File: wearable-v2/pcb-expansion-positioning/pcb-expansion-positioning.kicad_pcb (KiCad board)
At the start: 2 copper layers, 35.1 x 19 mm, 18 parts, among them IC1 TESEO-LIV3F, J8 HERALD_V2_CONN_PLUG, U14 LIS2DE12

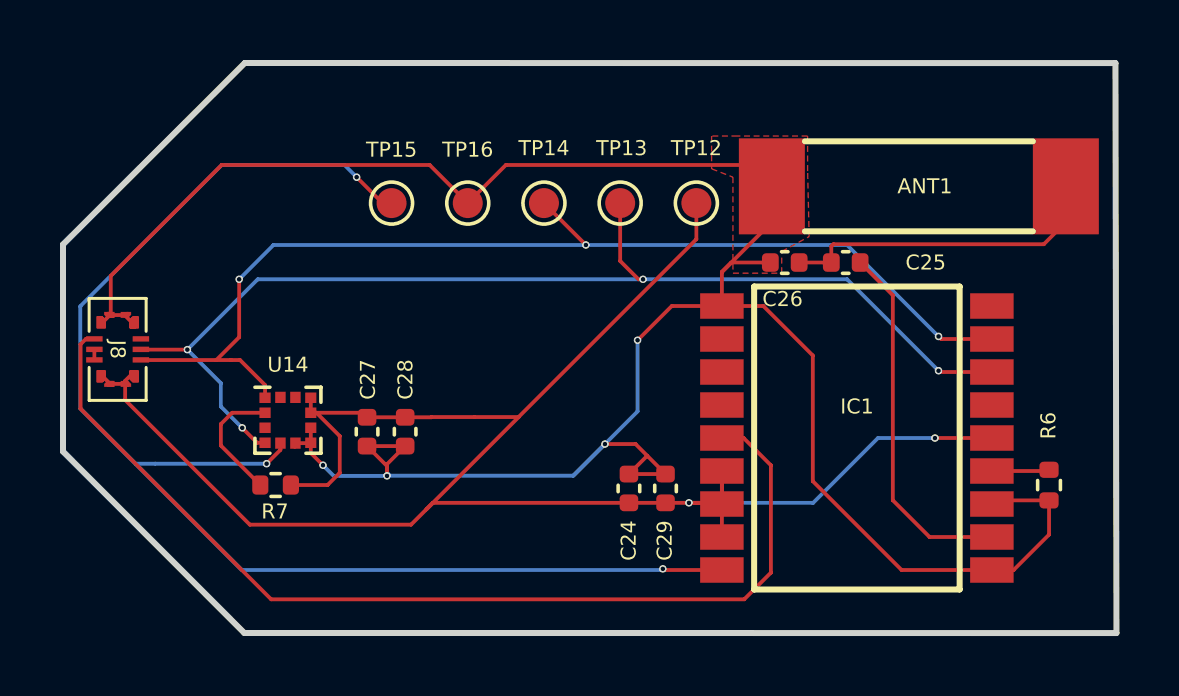
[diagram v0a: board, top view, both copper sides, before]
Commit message: Reworked boards for JLCPCB manufacture
Slightly larger Vias.
Added debug pin holes for Beta testing.
Signed-off-by: Adam Fowler <adam@adamfowler.org>
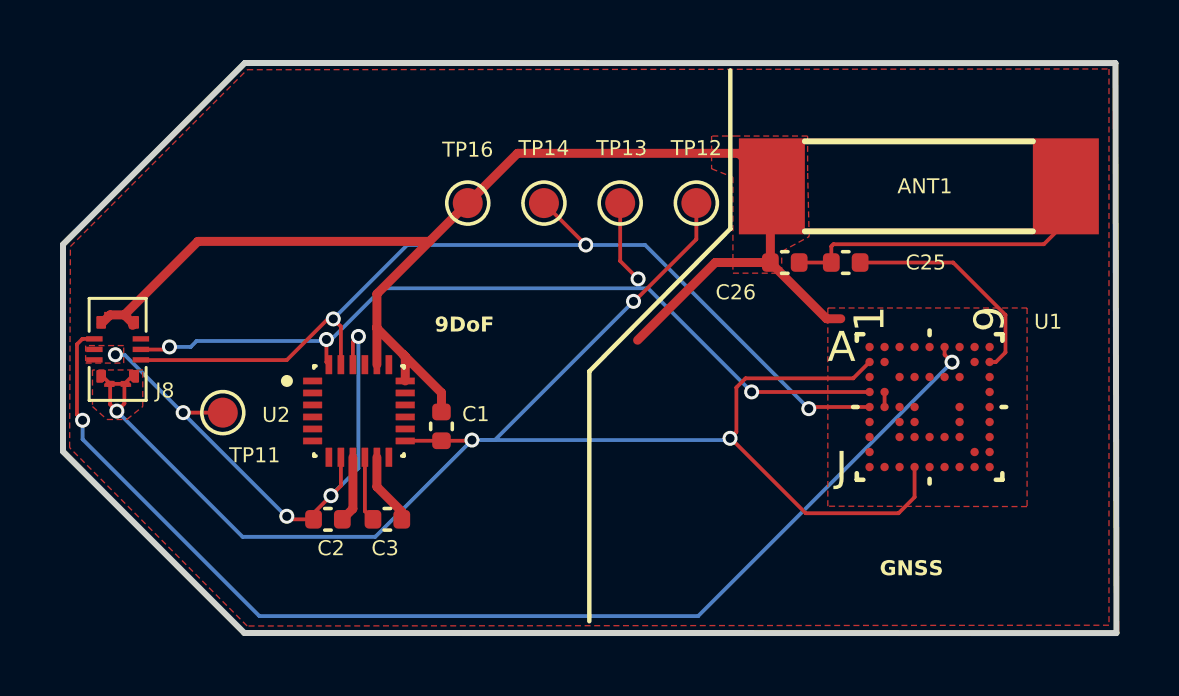
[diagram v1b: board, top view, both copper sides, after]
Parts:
- removed BoardPositioning: Board Positioning, PCM_kikit:Board
- removed C24: 56pF, Capacitor_SMD:C_0402_1005Metric
- removed C27: 10uF, Capacitor_SMD:C_0402_1005Metric
- removed C28, C29: 100nF, Capacitor_SMD:C_0402_1005Metric
- removed IC1: TESEO-LIV3F, Herald:SON110P970X1010X230-18N
- removed R6, R7: 10k, Resistor_SMD:R_0402_1005Metric
- removed TP15: POS_RESETn, TestPoint:TestPoint_Pad_D1.0mm
- removed U14: LIS2DE12, Package_LGA:LGA-12_2x2mm_P0.5mm
- added C1: 100nF, Capacitor_SMD:C_0402_1005Metric, F.Cu at (131.2, 99.1)
- added C2: 100nF, Capacitor_SMD:C_0402_1005Metric, F.Cu at (127.4, 102.2)
- added C3: 100nF, Capacitor_SMD:C_0402_1005Metric, F.Cu at (129.4, 102.2)
- added TP11: VDD1, TestPoint:TestPoint_Pad_D1.0mm, F.Cu at (123.9, 98.6)
- added U1: MIA-M10Q-00B, Herald:LGA_M10Q-00B_UBL, F.Cu at (147.5, 98.4)
- added U2: ICM-20948, Herald:ICM-20948-QFN40P300X300X105-24N, F.Cu at (128.4, 98.6)
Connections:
- J8 pad 1: VDD1 -> VDD
- J8 pad 2: /Positioning Board V1/VCC_1V8 -> VDD1
- J8 pad 4: /Positioning Board V1/VCC_1V8 -> VDD1
- TP12 pad 1: VDD1 -> VDD
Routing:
- net VDD: track 0.00 -> 55.6 mm, vias 0 -> 4
- net VDD1: track 64.9 -> 19.2 mm, vias 2 -> 5
- net /Positioning Board V1/POS_RESETn: track 45.2 -> 0.00 mm, vias 3 -> 0
- net GND: track 84.0 -> 50.9 mm, vias 4 -> 0
- net /Positioning Board V1/SDA: track 37.9 -> 30.2 mm
- net /Positioning Board V1/GNSS_INT: track 34.3 -> 39.4 mm, vias 0 -> 2
- net /Positioning Board V1/SCL: track 36.8 -> 31.8 mm
- net /Positioning Board V1/ANT_RF: track 12.2 -> 7.48 mm
- net Net-(U14-~{CS}): track 4.21 -> 0.00 mm
- net Net-(U2-REGOUT): track 0.00 -> 2.18 mm
- net Net-(IC1-ANT_OFF): track 1.92 -> 0.00 mm
- net Net-(U1-RESERVED-PadD2): track 0.00 -> 0.50 mm
- added copper zone on F.Cu, net VDD
- added copper zone on F.Cu, net VDD1
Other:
- board text added: "9DoF"
- board text added: "GNSS"

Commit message: Added Antenna panel and Micro connector boards
Micro connector uses the nPM1300 PMIC from Nordic Semi.
Signed-off-by: Adam Fowler <adam@adamfowler.org>
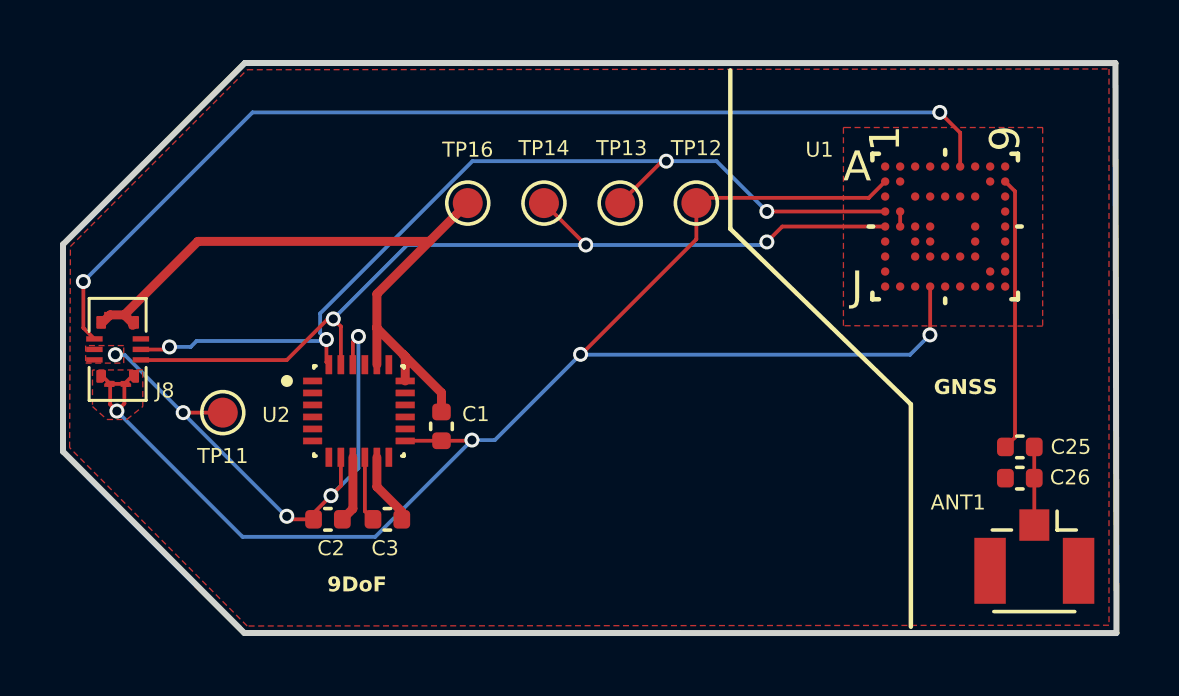
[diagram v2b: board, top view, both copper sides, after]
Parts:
- ANT1: footprint Herald:NN02-224 -> Connector_Coaxial:U.FL_Hirose_U.FL-R-SMT-1_Vertical
- moved ANT1 12.9 mm to (151.0, 103.4), turned to -90 degrees
- moved C26 10.6 mm to (150.5, 100.8)
- moved C25 8.45 mm to (150.5, 99.8), turned to 0 degrees
- moved U1 6.04 mm to (148.0, 92.4)
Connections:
- ANT1 pad 2: GND -> (no net)
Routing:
- net GND: track 50.9 -> 28.4 mm
- net Net-(ANT1-Pad1): track 9.90 -> 2.61 mm
- net /Positioning Board V1/GNSS_INT: track 39.4 -> 35.0 mm
- net VDD: track 55.6 -> 52.2 mm
- net /Positioning Board V1/ANT_RF: track 7.48 -> 9.12 mm
- net /Positioning Board V1/SDA: track 30.2 -> 31.9 mm
- net /Positioning Board V1/SCL: track 31.8 -> 30.3 mm
